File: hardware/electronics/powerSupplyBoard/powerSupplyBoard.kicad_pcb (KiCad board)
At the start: 4 copper layers, 118 parts, among them J1 USB_C_Receptacle_USB2.0, J10 PREC002SAAN-RC, J11 S2B-PH-SM4-TB, J2 XT60PW-M, J3 S3B-XH-SM4-TB, J4 1729018, J5 Barrel_Jack_Switch, J6 PRPC009SBAN-M71RC, J8 PREC002SAAN-RC, J9 PREC003SAAN-RC, Q1 BUK961R6, Q2 CSD18532Q5B, Q3 CSD18532Q5B, Q4 BSS84, Q5 2N7002, Q6 2N7002, SW1 PTS647, SW2 SS-12D07, U1 STM32L052K6, U2 AP2112K-3.3, U3 SN65HVD230QDR, U4 BQ25798, U5 BQ76905, U6 BQ34Z100-R2, Y1 ECS-327ATQMV

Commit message: added footprints to project lib
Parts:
- C1, C2, C31, C32, C34, C47, C6: footprint DS-Capacitors-SMD:MLCC0805 -> lib_fp:MLCC0805
- C10, C11, C14, C15, C19, C27, C28, C29, C3, C33, C35, C36, C37, C38, C39, C4, C40, C41, C42, C43, C44, C45, C46, C5, C7, C8, C9: footprint DS-Capacitors-SMD:MLCC0603 -> lib_fp:MLCC0603
- C12, C13, C16, C17, C18, C20, C21, C22, C23, C24, C25, C26, C30: footprint DS-Capacitors-SMD:MLCC1206 -> lib_fp:MLCC1206
- D1: footprint DS-LED-SMD:LTST-1206 -> lib_fp:LTST-1206
- D2, D3, D4: footprint DS-Package-SO:SOD123 -> lib_fp:SOD123
- D6: footprint DS-Package-SO:SOD523 -> lib_fp:SOD523
- F1: footprint DS-Fuses:PTS1206 -> lib_fp:PTS1206
- J1: footprint DS-Connector-USB:MOLEX_2171790001 -> lib_fp:MOLEX_2171790001
- J10, J8: footprint DS-Rectangular-Connectors:conn_01x02_254 -> lib_fp:conn_01x02_254
- J11: footprint DS-Rectangular-Connectors:JST-PH-S2B-SM4-TB -> lib_fp:JST-PH-S2B-SM4-TB
- J2: footprint DS-Battery-Connectors:AMASS_XT60PW-M -> lib_fp:AMASS_XT60PW-M
- J3: footprint DS-Rectangular-Connectors:JST_XH_S3B-SM4-TB -> lib_fp:JST_XH_S3B-SM4-TB
- J4: footprint DS-Rectangular-Connectors:5mmTerminalBlock -> lib_fp:5mmTerminalBlock
- J5: footprint DS-Battery-Connectors:PJ-002A -> lib_fp:PJ-002A
- J6: footprint DS-Rectangular-Connectors:conn_01x09_254_right_angle -> lib_fp:conn_01x09_254_right_angle
- J7: footprint DS-Connectors-SMD:TC2050-FP -> lib_fp:TC2050-FP
- J9: footprint DS-Rectangular-Connectors:conn_01x03_254 -> lib_fp:conn_01x03_254
- L1: footprint DS-Inductors-SMD:HCM1A1105V2 -> lib_fp:HCM1A1105V2
- NT1, NT2: footprint DS-Resistors-SMD:CRCW1210 -> lib_fp:CRCW1210
- Q1: footprint DS-Package-SO:SOT404 -> lib_fp:SOT404
- Q2, Q3: footprint DS-Package-SO:SON8P127_500X600X100L56X41N -> lib_fp:SON8P127_500X600X100L56X41N
- Q4, Q5, Q6: footprint DS-Package-SO:SOT23-3P95_290X130L43X40N -> lib_fp:SOT23-3P95_290X130L43X40N
- R1, R10, R11, R12, R13, R14, R15, R16, R17, R18, R2, R20, R21, R22, R23, R24, R28, R29, R3, R31, R32, R33, R34, R35, R36, R4, R5, R6, R7, R8, R9: footprint DS-Resistors-SMD:CRCW0603 -> lib_fp:CRCW0603
- R19, R30: footprint DS-Resistors-SMD:WSLHP2010 -> lib_fp:WSLHP2010
- R25, R26, R27: footprint DS-Resistors-SMD:CRCW1206 -> lib_fp:CRCW1206
- SW1: footprint DS-Switches:SW_4.5x4.5 -> lib_fp:SW_4.5x4.5
- SW2: footprint DS-Switches:SS-12D07-VG_GA_PA -> lib_fp:SS-12D07-VG_GA_PA
- U1: footprint DS-Microcontrollers:UFQFPN32 -> lib_fp:UFQFPN32
- U2: footprint DS-Package-SO:SOT23-5P95_280X300X110L40X38N -> lib_fp:SOT23-5P95_280X300X110L40X38N
- U3: footprint DS-Package-SO:SOIC8P127_490X600X195L83X42N -> lib_fp:SOIC8P127_490X600X195L83X42N
- U4: footprint DS-PMIC-SMD:RQM0029A -> lib_fp:RQM0029A
- U5: footprint DS-PMIC-SMD:RGR0020A -> lib_fp:RGR0020A
- U6: footprint DS-Package-SO:TSSOP14P65_500x640X120L150X45N -> lib_fp:TSSOP14P65_500x640X120L150X45N
- Y1: footprint DS-Crystals:EXC-34Q -> lib_fp:EXC-34Q

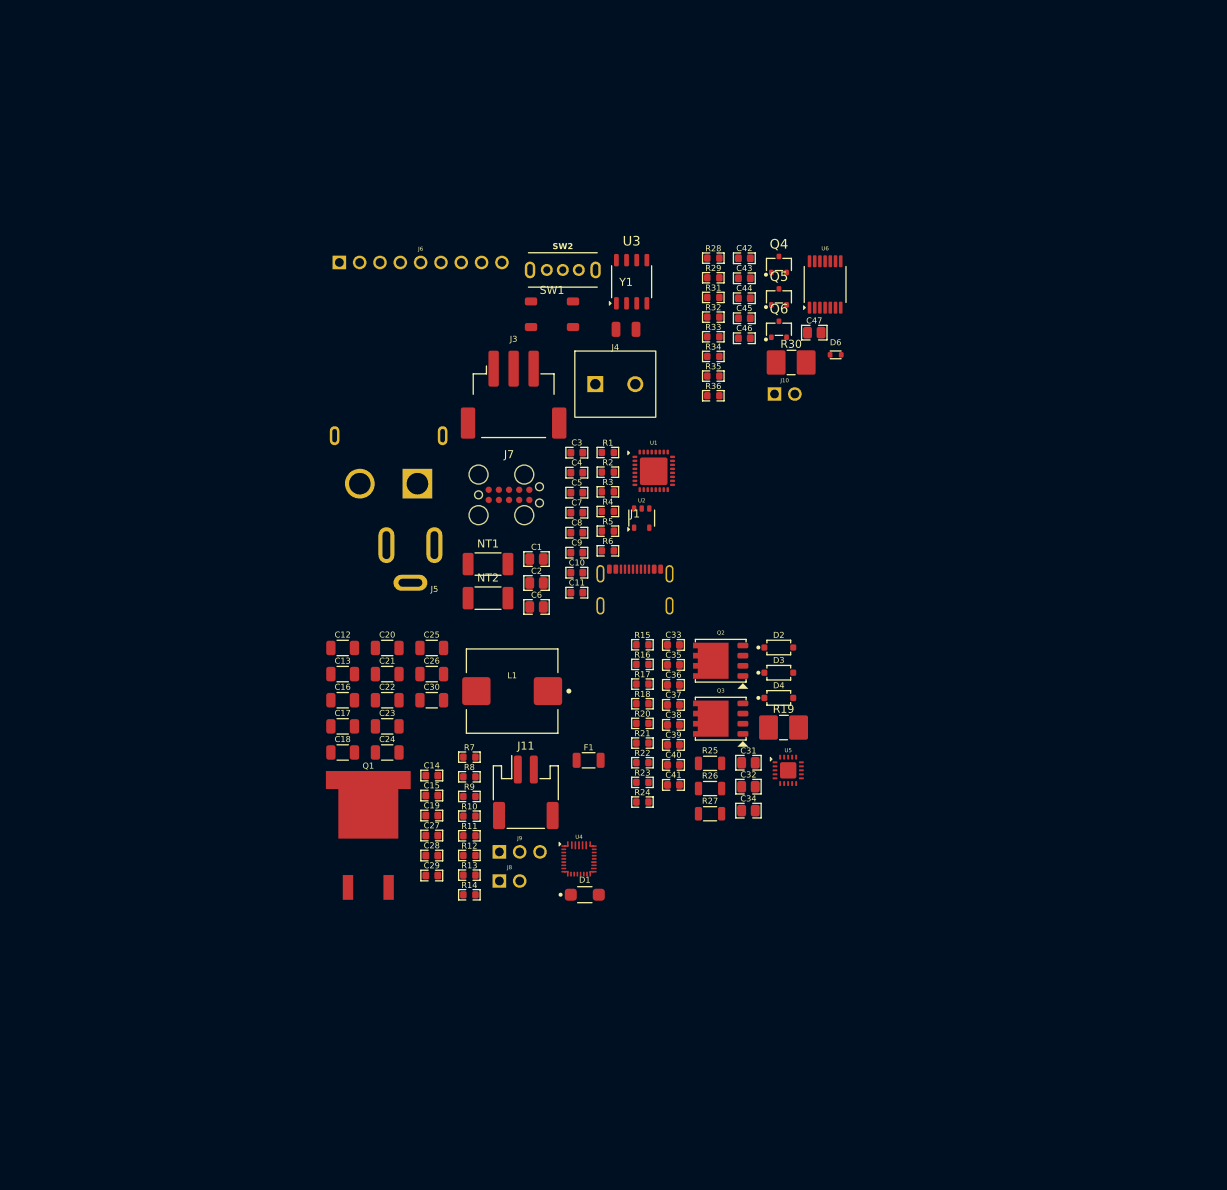
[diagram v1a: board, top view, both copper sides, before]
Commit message: added board outline and internal ground planes
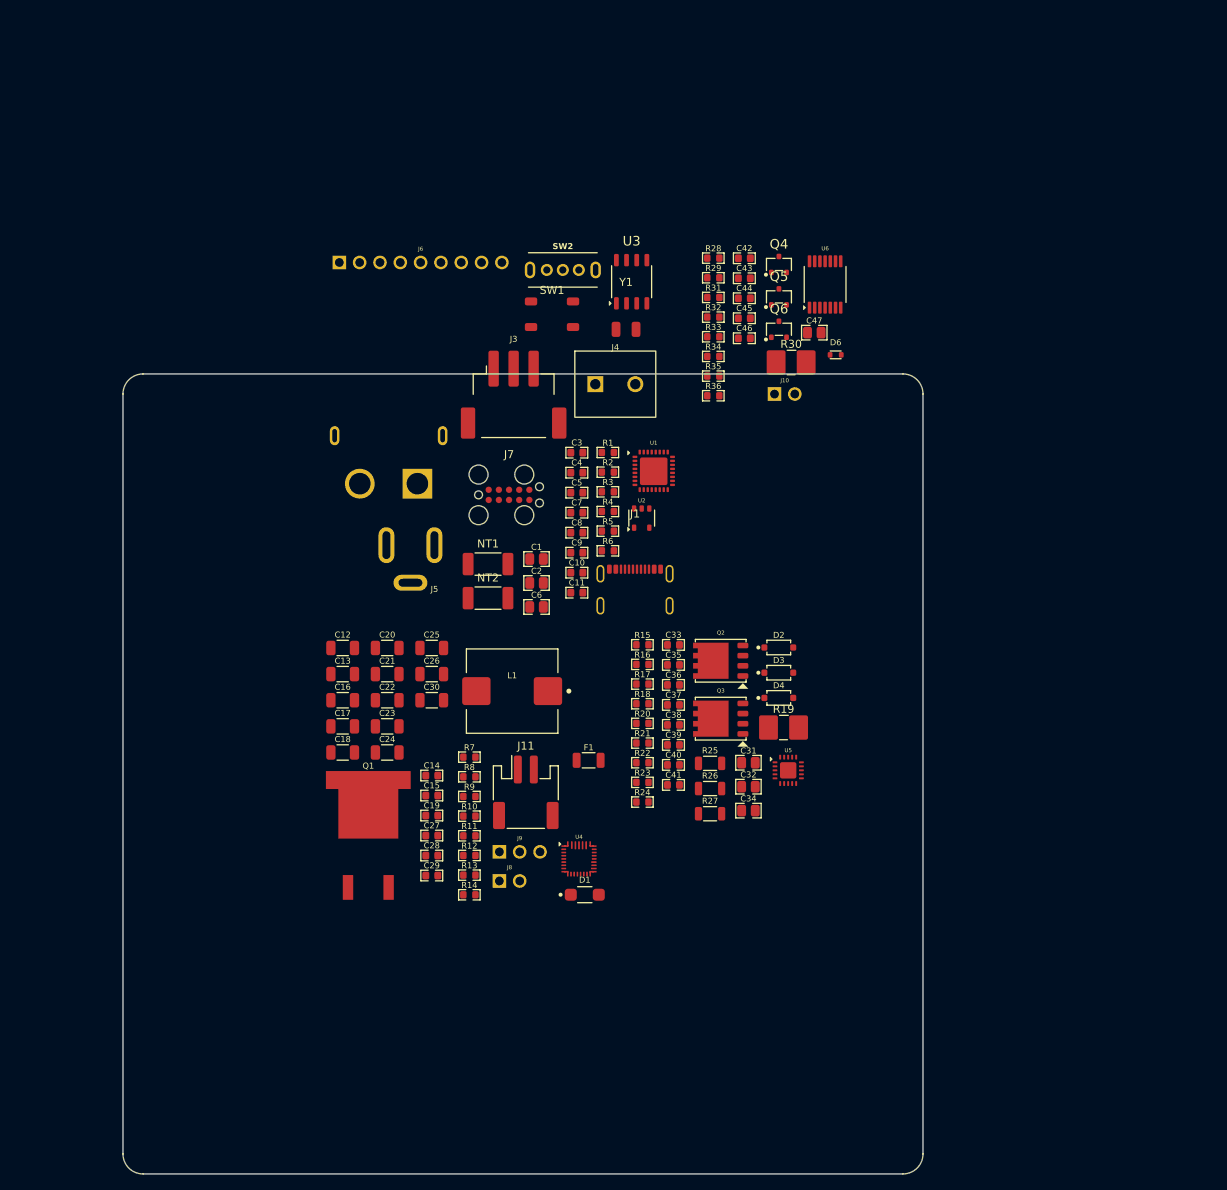
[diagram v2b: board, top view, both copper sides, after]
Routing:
- added copper zone on In1.Cu, net GND
- added copper zone on In2.Cu, net GND
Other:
- board outline added: 100 x 100 mm
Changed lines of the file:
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@@
+		)
+	)
+	(gr_line
+		(start 92.2 157.95)
+		(end 187.2 157.95)
+		(locked yes)
+		(stroke
+			(width 0.05)
+			(type default)
+		)
+		(layer "Edge.Cuts")
+	)
+	(gr_arc
+		(start 89.7 60.45)
+		(mid 90.432233 58.682233)
+		(end 92.2 57.95)
+		(locked yes)
+		(stroke
+			(width 0.05)
+			(type default)
+		)
+		(layer "Edge.Cuts")
+	)
+	(gr_line
+		(start 187.2 57.95)
+		(end 92.2 57.95)
+		(locked yes)
+		(stroke
+			(width 0.05)
+			(type default)
+		)
+		(layer "Edge.Cuts")
+	)
+	(gr_arc
+		(start 189.7 155.45)
+		(mid 188.967767 157.217767)
+		(end 187.2 157.95)
+		(locked yes)
+		(stroke
+			(width 0.05)
+			(type default)
+		)
+		(layer "Edge.Cuts")
+	)
+	(gr_line
+		(start 89.7 60.45)
+		(end 89.7 155.45)
+		(locked yes)
+		(stroke
+			(width 0.05)
+			(type default)
+		)
+		(layer "Edge.Cuts")
+	)
+	(gr_arc
+		(start 92.2 157.95)
+		(mid 90.432233 157.217767)
+		(end 89.7 155.45)
+		(locked yes)
+		(stroke
+			(width 0.05)
+			(type default)
+		)
+		(layer "Edge.Cuts")
+	)
+	(gr_arc
+		(start 187.2 57.95)
+		(mid 188.967767 58.682233)
+		(end 189.7 60.45)
+		(locked yes)
+		(stroke
+			(width 0.05)
+			(type default)
+		)
+		(layer "Edge.Cuts")
+	)
+	(gr_line
+		(start 189.7 155.45)
+		(end 189.7 60.45)
+		(locked yes)
+		(stroke
+			(width 0.05)
+			(type default)
+		)
+		(layer "Edge.Cuts")
+	)
+	(zone
+		(net 2)
+		(net_name "GND")
+		(locked yes)
+		(layers "In1.Cu" "In2.Cu")
+		(hatch edge 0.5)
+		(connect_pads
+			(clearance 0.5)
+		)
+		(min_thickness 0.25)
+		(filled_areas_thickness no)
+		(fill yes
+			(thermal_gap 0.5)
+			(thermal_bridge_width 0.5)
+		)
+		(polygon
+			(pts
+				(xy 189.7 157.95) (xy 189.7 57.95) (xy 89.7 57.95) (xy 89.7 157.95)
+			)
 		)
 	)

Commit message: started layout of uC
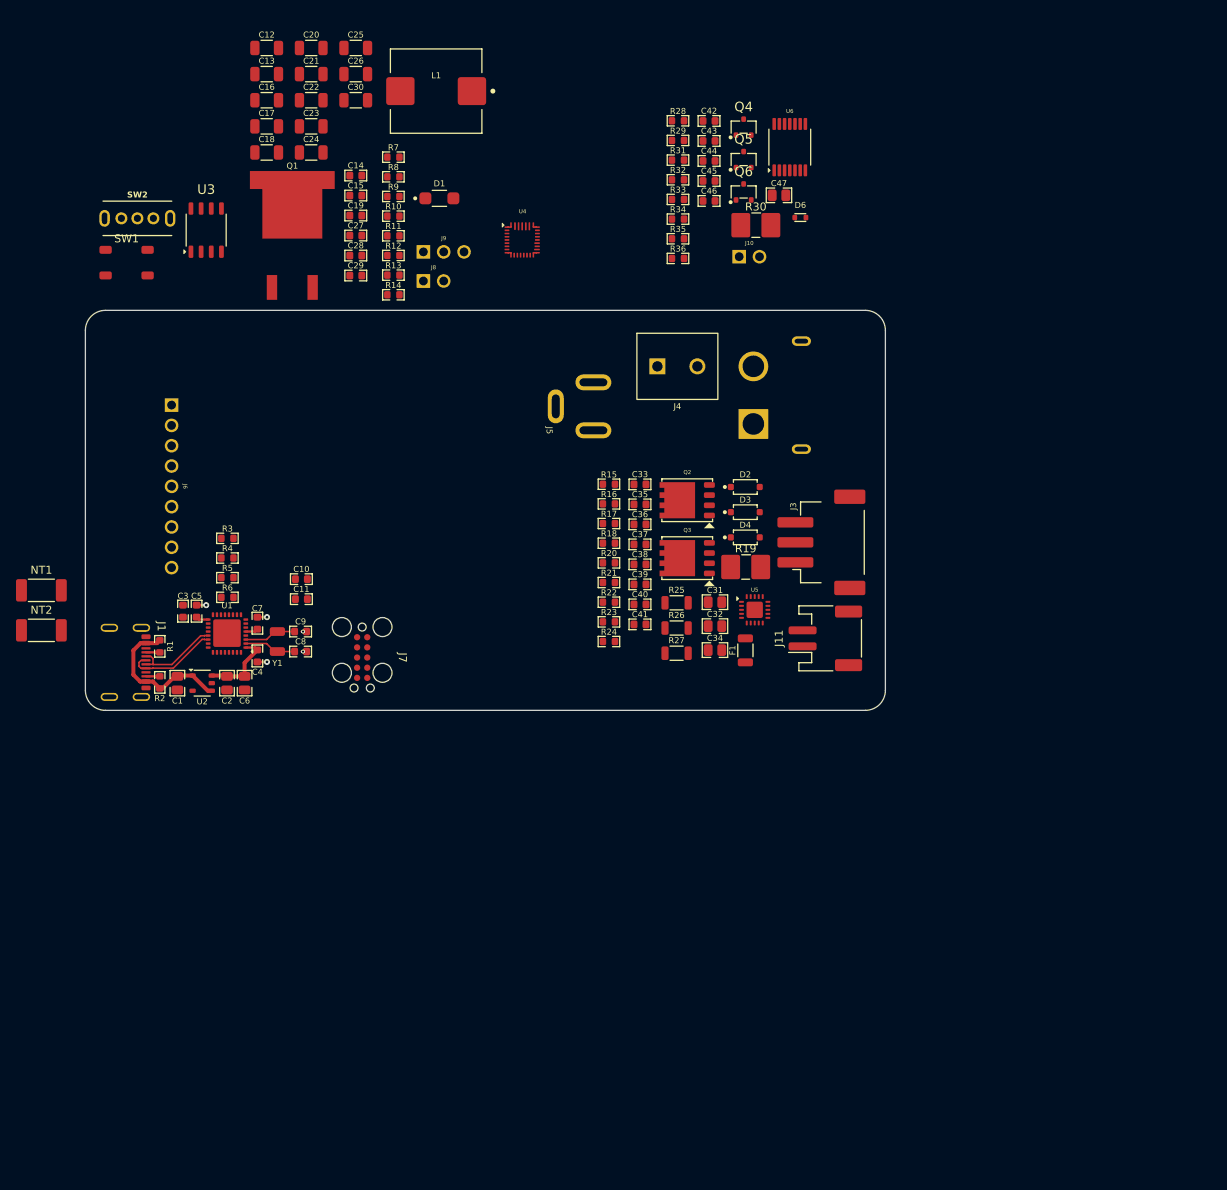
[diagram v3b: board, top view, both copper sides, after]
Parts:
- C1, C2, C31, C32, C34, C47, C6: footprint lib_fp:MLCC0805 -> DS-Capacitors-SMD:MLCC0805
- C10, C11, C14, C15, C19, C27, C28, C29, C3, C33, C35, C36, C37, C38, C39, C4, C40, C41, C42, C43, C44, C45, C46, C5, C7, C8, C9: footprint lib_fp:MLCC0603 -> DS-Capacitors-SMD:MLCC0603
- C12, C13, C16, C17, C18, C20, C21, C22, C23, C24, C25, C26, C30: footprint lib_fp:MLCC1206 -> DS-Capacitors-SMD:MLCC1206
- D1: footprint lib_fp:LTST-1206 -> DS-LED-SMD:LTST-1206
- D2, D3, D4: footprint lib_fp:SOD123 -> DS-Package-SO:SOD123
- D6: footprint lib_fp:SOD523 -> DS-Package-SO:SOD523
- F1: footprint lib_fp:PTS1206 -> DS-Fuses:PTS1206
- J1: footprint lib_fp:MOLEX_2171790001 -> DS-Connector-USB:MOLEX_2171790001
- J10, J8: footprint lib_fp:conn_01x02_254 -> DS-Rectangular-Connectors:conn_01x02_254
- J11: footprint lib_fp:JST-PH-S2B-SM4-TB -> DS-Rectangular-Connectors:JST-PH-S2B-SM4-TB
- J2: footprint lib_fp:AMASS_XT60PW-M -> DS-Battery-Connectors:AMASS_XT60PW-M
- J3: footprint lib_fp:JST_XH_S3B-SM4-TB -> DS-Rectangular-Connectors:JST_XH_S3B-SM4-TB
- J4: footprint lib_fp:5mmTerminalBlock -> DS-Rectangular-Connectors:5mmTerminalBlock
- J5: footprint lib_fp:PJ-002A -> DS-Battery-Connectors:PJ-002A
- J6: footprint lib_fp:conn_01x09_254_right_angle -> DS-Rectangular-Connectors:conn_01x09_254_right_angle
- J7: footprint lib_fp:TC2050-FP -> DS-Connectors-SMD:TC2050-FP
- J9: footprint lib_fp:conn_01x03_254 -> DS-Rectangular-Connectors:conn_01x03_254
- L1: footprint lib_fp:HCM1A1105V2 -> DS-Inductors-SMD:HCM1A1105V2
- NT1, NT2: footprint lib_fp:CRCW1210 -> DS-Resistors-SMD:CRCW1210
- Q1: footprint lib_fp:SOT404 -> DS-Package-SO:SOT404
- Q2, Q3: footprint lib_fp:SON8P127_500X600X100L56X41N -> DS-Package-SO:SON8P127_500X600X100L56X41N
- Q4, Q5, Q6: footprint lib_fp:SOT23-3P95_290X130L43X40N -> DS-Package-SO:SOT23-3P95_290X130L43X40N
- R1, R10, R11, R12, R13, R14, R15, R16, R17, R18, R2, R20, R21, R22, R23, R24, R28, R29, R3, R31, R32, R33, R34, R35, R36, R4, R5, R6, R7, R8, R9: footprint lib_fp:CRCW0603 -> DS-Resistors-SMD:CRCW0603
- R19, R30: footprint lib_fp:WSLHP2010 -> DS-Resistors-SMD:WSLHP2010
- R25, R26, R27: footprint lib_fp:CRCW1206 -> DS-Resistors-SMD:CRCW1206
- SW1: footprint lib_fp:SW_4.5x4.5 -> DS-Switches:SW_4.5x4.5
- SW2: footprint lib_fp:SS-12D07-VG_GA_PA -> DS-Switches:SS-12D07-VG_GA_PA
- U1: footprint lib_fp:UFQFPN32 -> DS-Microcontrollers:UFQFPN32
- U2: footprint lib_fp:SOT23-5P95_280X300X110L40X38N -> DS-Package-SO:SOT23-5P95_280X300X110L40X38N
- U3: footprint lib_fp:SOIC8P127_490X600X195L83X42N -> DS-Package-SO:SOIC8P127_490X600X195L83X42N
- U4: footprint lib_fp:RQM0029A -> DS-PMIC-SMD:RQM0029A
- U5: footprint lib_fp:RGR0020A -> DS-PMIC-SMD:RGR0020A
- U6: footprint lib_fp:TSSOP14P65_500x640X120L150X45N -> DS-Package-SO:TSSOP14P65_500x640X120L150X45N
- Y1: footprint lib_fp:EXC-34Q -> DS-Crystals:EXC-34Q
- moved D1 88.9 mm to (129.2, 36.0)
- moved U4 77.7 mm to (139.6, 41.2)
- moved C12 75.6 mm to (107.7, 17.2)
- moved C13 75.6 mm to (107.7, 20.5)
- moved C14 75.6 mm to (118.8, 33.1)
- moved C15 75.6 mm to (118.8, 35.6)
- moved C16 75.6 mm to (107.7, 23.7)
- moved C17 75.6 mm to (107.7, 27.0)
- moved C18 75.6 mm to (107.7, 30.3)
- moved C19 75.6 mm to (118.8, 38.1)
- moved C20 75.6 mm to (113.2, 17.2)
- moved C21 75.6 mm to (113.2, 20.5)
- moved C22 75.6 mm to (113.2, 23.7)
- moved C23 75.6 mm to (113.2, 27.0)
- moved C24 75.6 mm to (113.2, 30.3)
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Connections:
- C1 pad 1: /VBUS -> /VUSB
- J1 pad A4: /VBUS -> /VUSB
- J1 pad A9: /VBUS -> /VUSB
- J1 pad B4: /VBUS -> /VUSB
- J1 pad B9: /VBUS -> /VUSB
- R1 pad 1: /VBUS -> /VUSB
- R2 pad 1: /VBUS -> /VUSB
- U2 pad 1: /VBUS -> /VUSB
- U2 pad 3: /VBUS -> /VUSB
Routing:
- net /VUSB: track 0.00 -> 18.8 mm
- net +3V3: track 0.00 -> 12.8 mm
- net /D_P: track 0.00 -> 11.7 mm
- net /D_N: track 0.00 -> 11.0 mm
- net Net-(U1-PC15-OSC32_OUT): track 0.00 -> 6.51 mm
- net Net-(U1-PC14-OSC32_IN): track 0.00 -> 6.51 mm
- net GND: track 0.00 -> 5.70 mm, vias 0 -> 5
- net Net-(J1-CC1): track 0.00 -> 1.73 mm
- net Net-(J1-CC2): track 0.00 -> 1.72 mm
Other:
- board size 100 x 100 mm -> 100 x 50 mm
